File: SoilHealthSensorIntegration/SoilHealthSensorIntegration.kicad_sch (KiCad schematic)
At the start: 11 parts, among them U1 ESP32-S2-SOLO-N4, U3 LP87334DRHDR

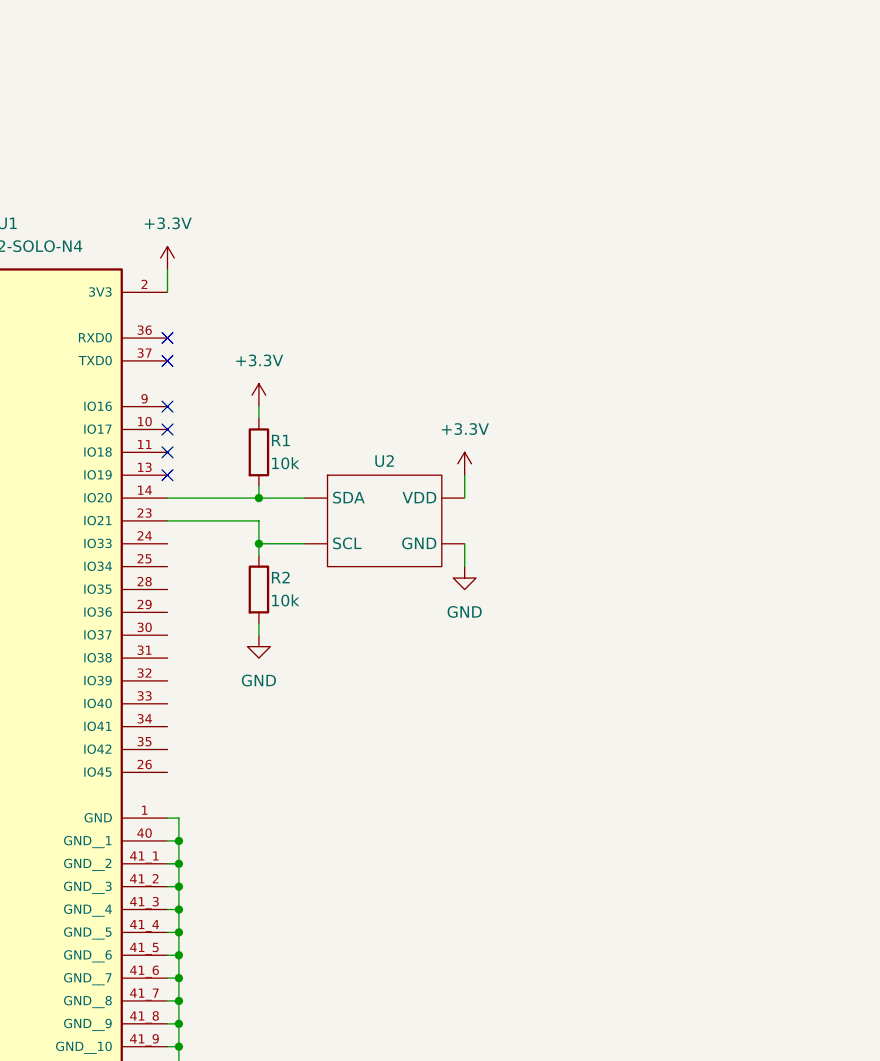
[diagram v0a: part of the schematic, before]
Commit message: Added USB C Connection + USB Comm with ESP32
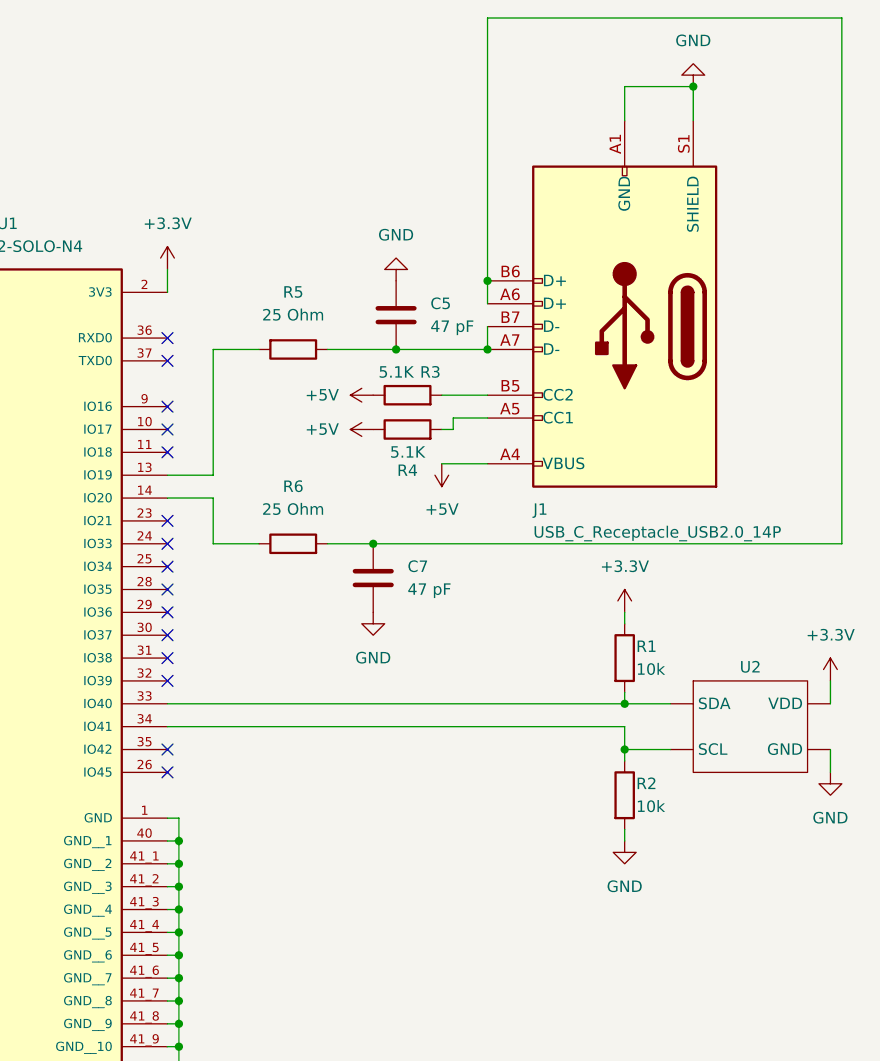
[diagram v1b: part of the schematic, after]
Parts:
- added C5, C7: 47 pF, symbol Device:C
- added J1: USB_C_Receptacle_USB2.0_14P, symbol Connector:USB_C_Receptacle_USB2.0_14P
- added R3, R4: 5.1K, symbol Device:R
- added R5, R6: 25 Ohm, symbol Device:R
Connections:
- net GND: now also C5.1, C7.2, J1.A1 (GND), J1.A12 (GND), J1.B1 (GND), J1.B12 (GND), J1.S1 (SHIELD)
- net at U1.13 (IO19): now also R5.2
- net at U1.33 (IO40): now also R1.2, U2. (VDD)
- net at U1.34 (IO41): now also R2.1, U2. (VDD)
- new net: R6.1, U1.14 (IO20)
- new net: C7.1, J1.A6 (D+), J1.B6 (D+), R6.2
- new net: J1.A5 (CC1), R4.2
- new net: C5.2, J1.A7 (D-), J1.B7 (D-), R5.1
- new net: J1.B5 (CC2), R3.2
- new net +5V: J1.A4 (VBUS), J1.A9 (VBUS), J1.B4 (VBUS), J1.B9 (VBUS), R3.1, R4.1
- now unconnected: U1.23 (IO21)
- no-connect marks 37 -> 46
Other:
- moved on the sheet: R1, R2, U2

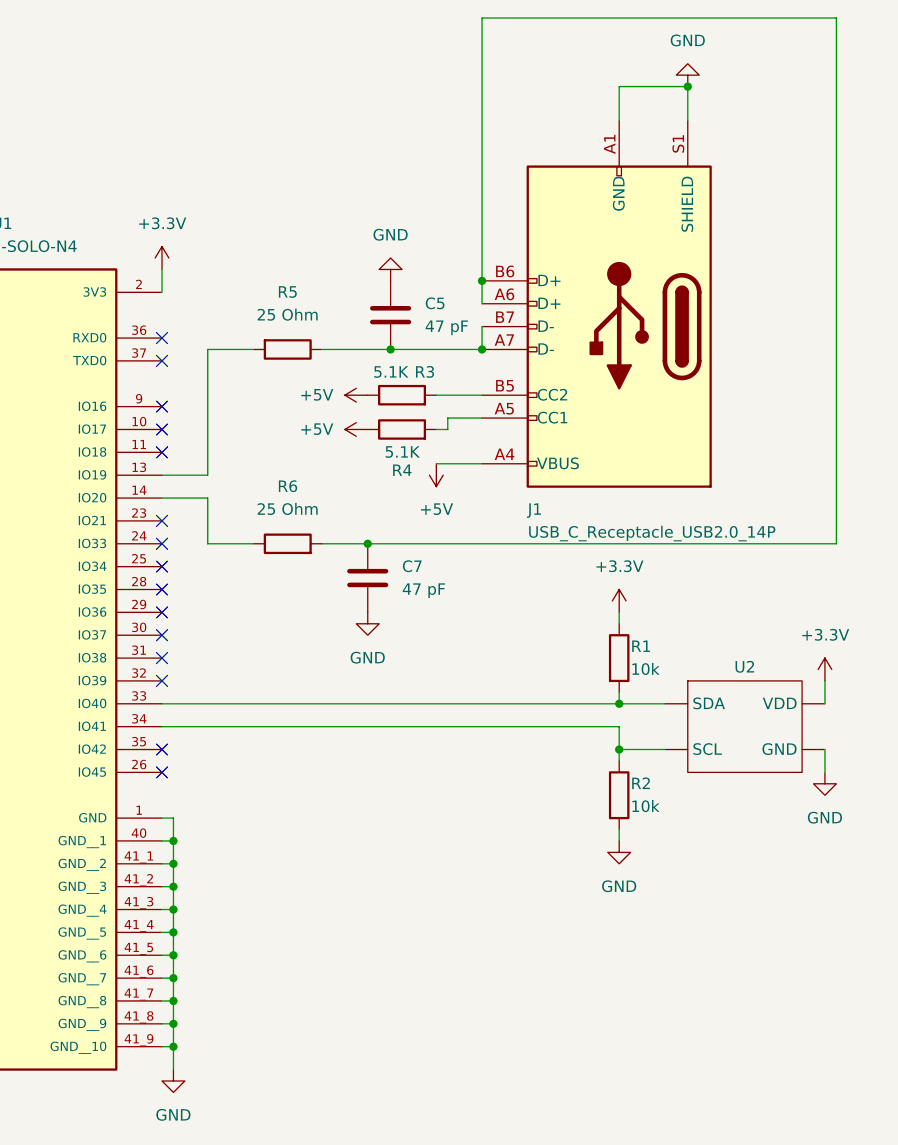
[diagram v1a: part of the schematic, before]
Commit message: Added PullUp and PullDown Resistors just in case
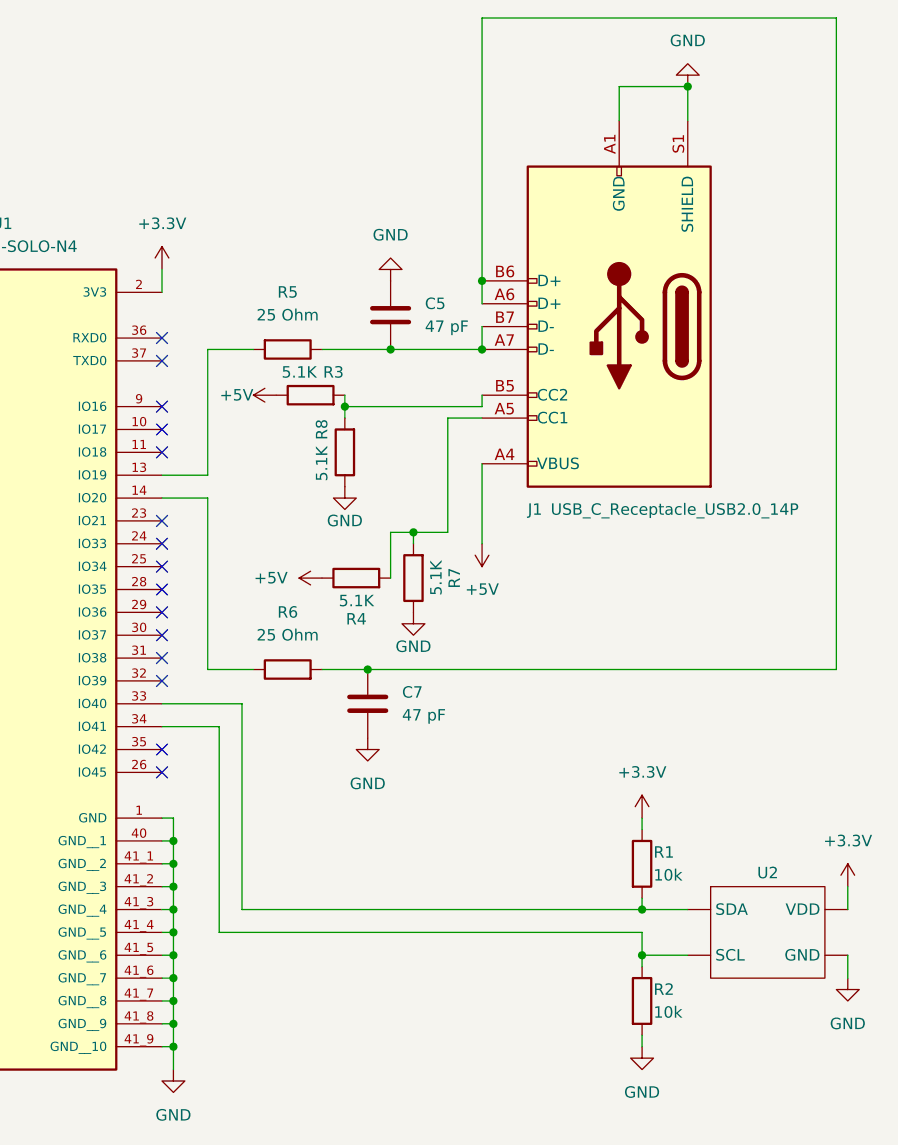
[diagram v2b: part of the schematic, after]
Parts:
- added R7, R8: 5.1K, symbol Device:R
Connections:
- net GND: now also R7.1, R8.1
- net at J1.A5 (CC1), R4.2: now also R7.2
- net at J1.B5 (CC2), R3.2: now also R8.2
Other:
- moved on the sheet: C7, R1, R2, R3, R4, R6, U2

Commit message: fixed schem
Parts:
- C5: value 47 pF -> 47pF
- R5, R6: value 25 Ohm -> 25
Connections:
- net +3.7V is gone; now on net +5V: C1.1, C2.1, U3.11 (VIN_B1), U3.12 (VIN_B1), U3.24 (VIN_B0), U3.25 (VIN_B0), U3.5 (VANA)
- net +5V: now also R4.2; no longer R4.1
- net GND: now also C5.2; no longer C5.1
- net at C6.1, U3.1 (VOUT_LDO0): now also C3.1, C4.1, L1.2, U3.2 (FB_B0)
- net at J1.A5 (CC1), R7.2: now also R4.1; no longer R4.2
- net at J1.A7 (D-), J1.B7 (D-), R5.1: now also C5.1; no longer C5.2
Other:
- moved on the sheet: C5, C7, J1, L1, R3, R4, R5, R6, R7, R8
